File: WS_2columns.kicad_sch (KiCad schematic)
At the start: 28 parts

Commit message: change pixel count
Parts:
- added C181, C182: 100n, Capacitor_SMD:C_0201_0603Metric, symbol Device:C_Small
- added D173, D174: WS2812B, Critbit_lib:LED_WS2812B-2020_pinsRenumbered, symbol LED:WS2812B
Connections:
- net GND: now also C181.2, C182.2, D173.3 (VSS), D174.3 (VSS)
- net PWR: now also C181.1, C182.1, D173.1 (VDD), D174.1 (VDD)
- net at D17.4 (DIN): now also D173.2 (DOUT); no longer D15.2 (DOUT)
- net at D16.4 (DIN): now also D174.2 (DOUT); no longer D18.2 (DOUT)
- new net: D174.4 (DIN), D18.2 (DOUT)
- new net: D15.2 (DOUT), D173.4 (DIN)
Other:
- moved on the sheet: C11, C12, C13, C14, C15, C16, C17, C18, C19, C20, C21, C22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

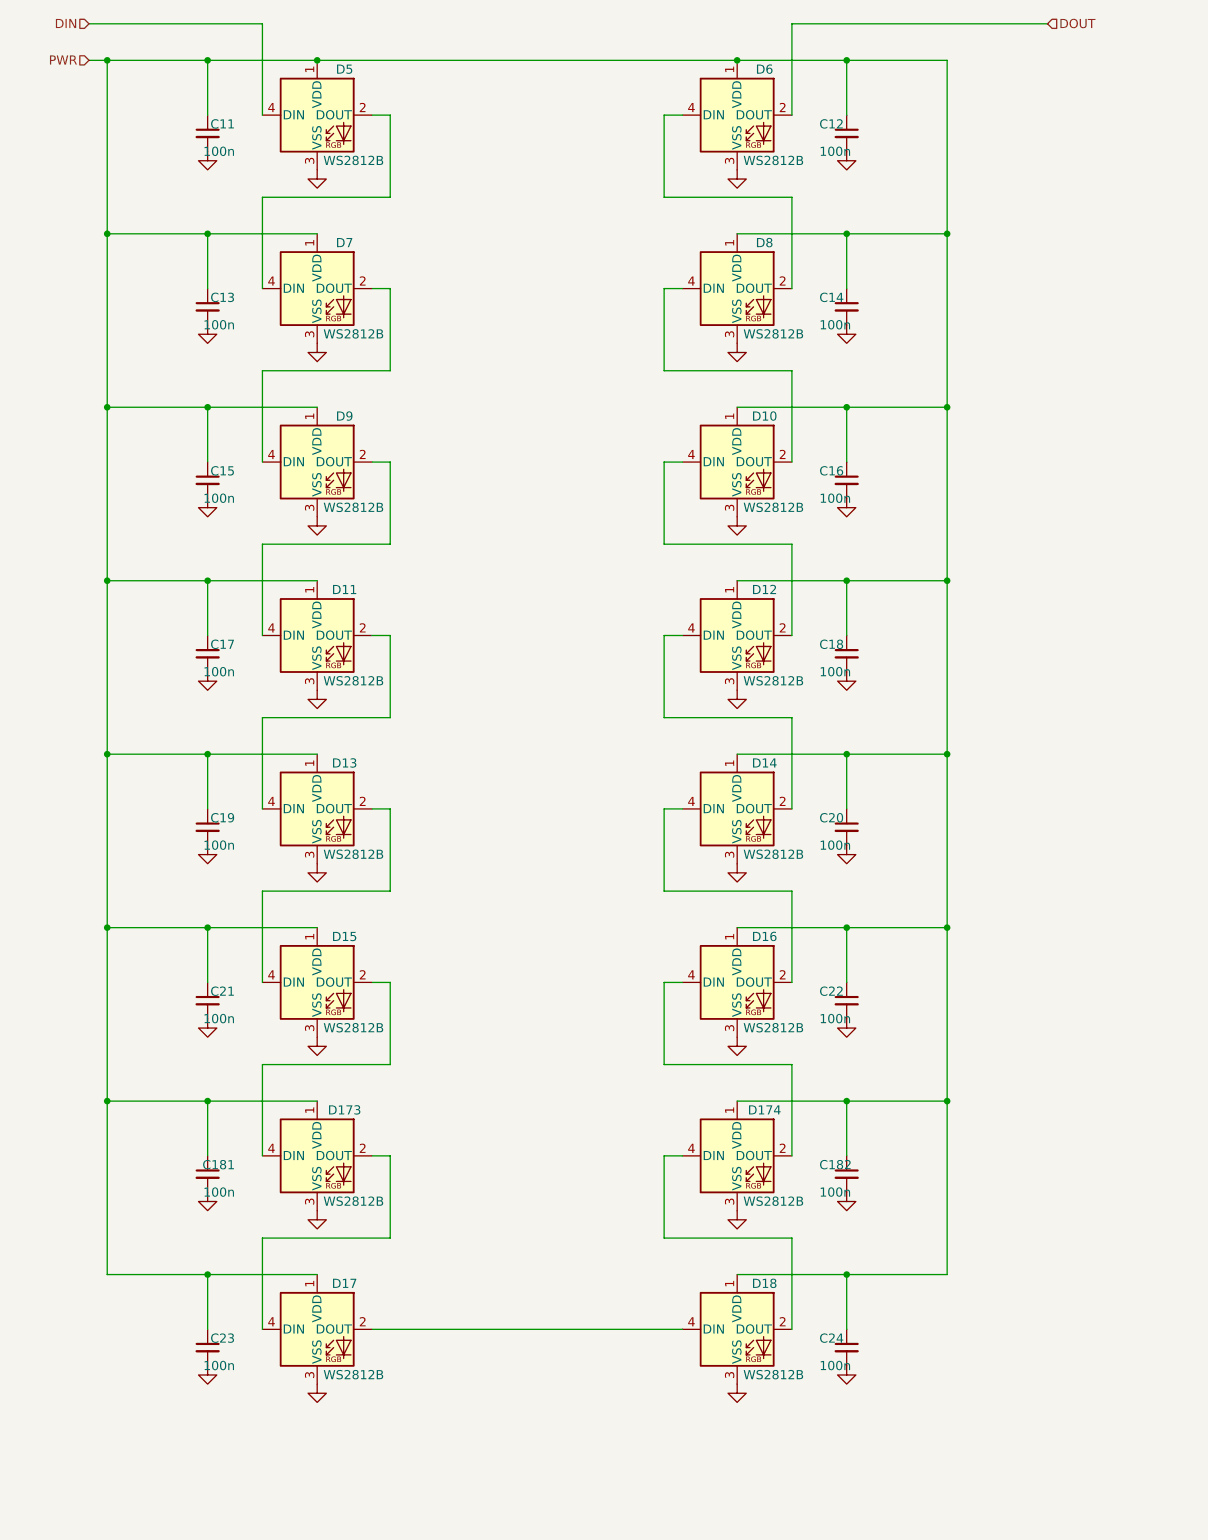
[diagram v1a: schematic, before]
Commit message: schematic cleanup, add PDF and 3D model
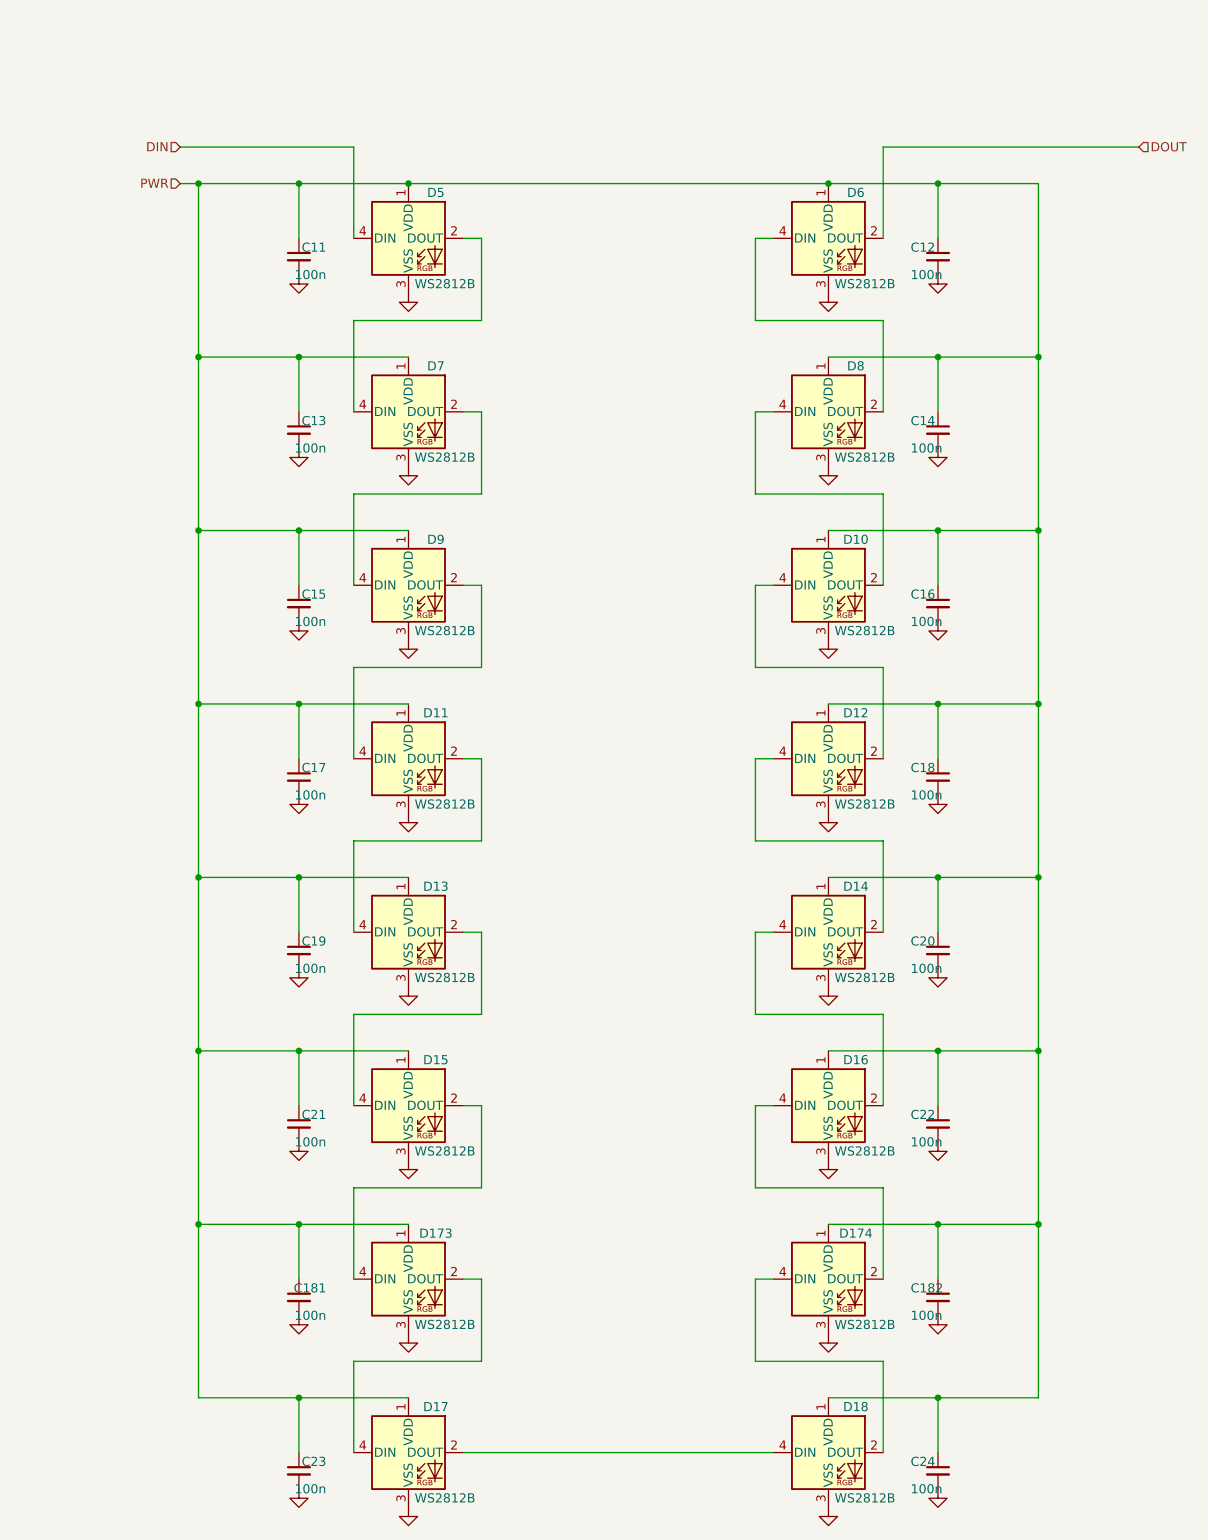
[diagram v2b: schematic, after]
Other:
- moved on the sheet: C11, C12, C13, C14, C15, C16, C17, C18, C181, C182, C19, C20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
